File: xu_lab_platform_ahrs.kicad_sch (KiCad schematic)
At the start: 0 parts

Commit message: Add 9DoF IMU and magnetometer sensors to sheet
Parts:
- added U2: ICM-20948, Sensor_Motion:InvenSense_QFN-24_3x3mm_P0.4mm, symbol Sensor_Motion:ICM-20948
- added U3: MMC5603NJ, Package_BGA:WLP-4_0.82X0.82mm_MEM, symbol XuLab:MMC5603NJ
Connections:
- new net: U2.18 (GND), U2.20 (GND)
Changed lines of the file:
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@@
 		(company "CU Boulder Senior Design Team 29 - Xu Lab")
 	)
+	(symbol
+		(lib_id "Sensor_Motion:ICM-20948")
+		(at 107.95 93.98 0)
+		(unit 1)
+		(exclude_from_sim no)
+		(in_bom yes)
+		(on_board yes)
+		(dnp no)
+		(fields_autoplaced yes)
+		(property "Reference" "U2"
+			(at 110.0933 111.76 0)
+			(effects
+				(font
+					(size 1.27 1.27)
+				)
+				(justify left)
+			)
+		)
+		(property "Value" "ICM-20948"
+			(at 110.0933 114.3 0)
+			(effects
+				(font
+					(size 1.27 1.27)
+				)
+				(justify left)
+			)
+		)
+		(property "Footprint" "Sensor_Motion:InvenSense_QFN-24_3x3mm_P0.4mm"
+			(at 107.95 119.38 0)
+			(effects
+				(font
+					(size 1.27 1.27)
+				)
+				(hide yes)
+			)
+		)
+		(property "Datasheet" "http://www.invensense.com/wp-content/uploads/2016/06/DS-000189-ICM-20948-v1.3.pdf"
+			(at 107.95 97.79 0)
+			(effects
+				(font
+					(size 1.27 1.27)
+				)
+				(hide yes)
+			)
+		)
+		(property "Description" "InvenSense 9-Axis Motion Sensor, Accelerometer, Gyroscope, Compass, I2C/SPI, QFN-24"
+			(at 107.95 93.98 0)
+			(effects
+				(font
+					(size 1.27 1.27)
+				)
+				(hide yes)
+			)
+		)
+		(pin "24"
+		)
+		(pin "23"
+		)
+		(pin "22"
+		)
+		(pin "15"
+		)
+		(pin "11"
+		)
+		(pin "12"
+		)
+		(pin "1"
+		)
+		(pin "2"
+		)
+		(pin "3"
+		)
+		(pin "4"
+		)
+		(pin "5"
+		)
+		(pin "8"
+		)
+		(pin "18"
+		)
+		(pin "20"
+		)
+		(pin "13"
+		)
+		(pin "6"
+		)
+		(pin "14"
+		)
+		(pin "9"
+		)
+		(pin "16"
+		)
+		(pin "17"
+		)
+		(pin "19"
+		)
+		(pin "21"
+		)
+		(pin "7"
+		)
+		(pin "10"
+		)
+		(instances
+			(project ""
+				(path "/71bb14ae-b730-4d22-a41d-cf68989dae2d/a5713b00-422c-456a-9938-13721b057665"
+					(reference "U2")
+					(unit 1)
+				)
+			)
+		)
+	)
+	(symbol
+		(lib_id "XuLab:MMC5603NJ")
+		(at 170.18 95.25 0)
+		(unit 1)
+		(exclude_from_sim no)
+		(in_bom yes)
+		(on_board yes)
+		(dnp no)
+		(fields_autoplaced yes)
+		(property "Reference" "U3"
+			(at 170.18 83.82 0)
+			(effects
+				(font
+					(size 1.524 1.524)
+				)
+			)
+		)
+		(property "Value" "MMC5603NJ"
+			(at 170.18 86.36 0)
+			(effects
+				(font
+					(size 1.524 1.524)
+				)
+			)
+		)
+		(property "Footprint" "Package_BGA:WLP-4_0.82X0.82mm_MEM"
+			(at 170.434 104.902 0)
+			(effects
+				(font
+					(size 1.27 1.27)
+					(italic yes)
+				)
+				(hide yes)
+			)
+		)
+		(property "Datasheet" "https://mm.digikey.com/Volume0/opasdata/d220001/medias/docus/333/MMC5603NJ_RevB_7-12-18.pdf"
+			(at 170.18 102.87 0)
+			(effects
+				(font
+					(size 1.27 1.27)
+					(italic yes)
+				)
+				(hide yes)
+			)
+		)
+		(property "Description" "he MMC5603NJ is a monolithic complete 3-axis AMR magnetic sensor with on-chip signal processing and integrated digital bus"
+			(at 170.18 107.95 0)
+			(effects
+				(font
+					(size 1.27 1.27)
+				)
+				(hide yes)
+			)
+		)
+		(pin "A1"
+		)
+		(pin "B2"
+		)
+		(pin "A2"
+		)
+		(pin "B1"
+		)
+		(instances
+			(project ""
+				(path "/71bb14ae-b730-4d22-a41d-cf68989dae2d/a5713b00-422c-456a-9938-13721b057665"
+					(reference "U3")
+					(unit 1)
+				)
+			)
+		)
+	)
 )

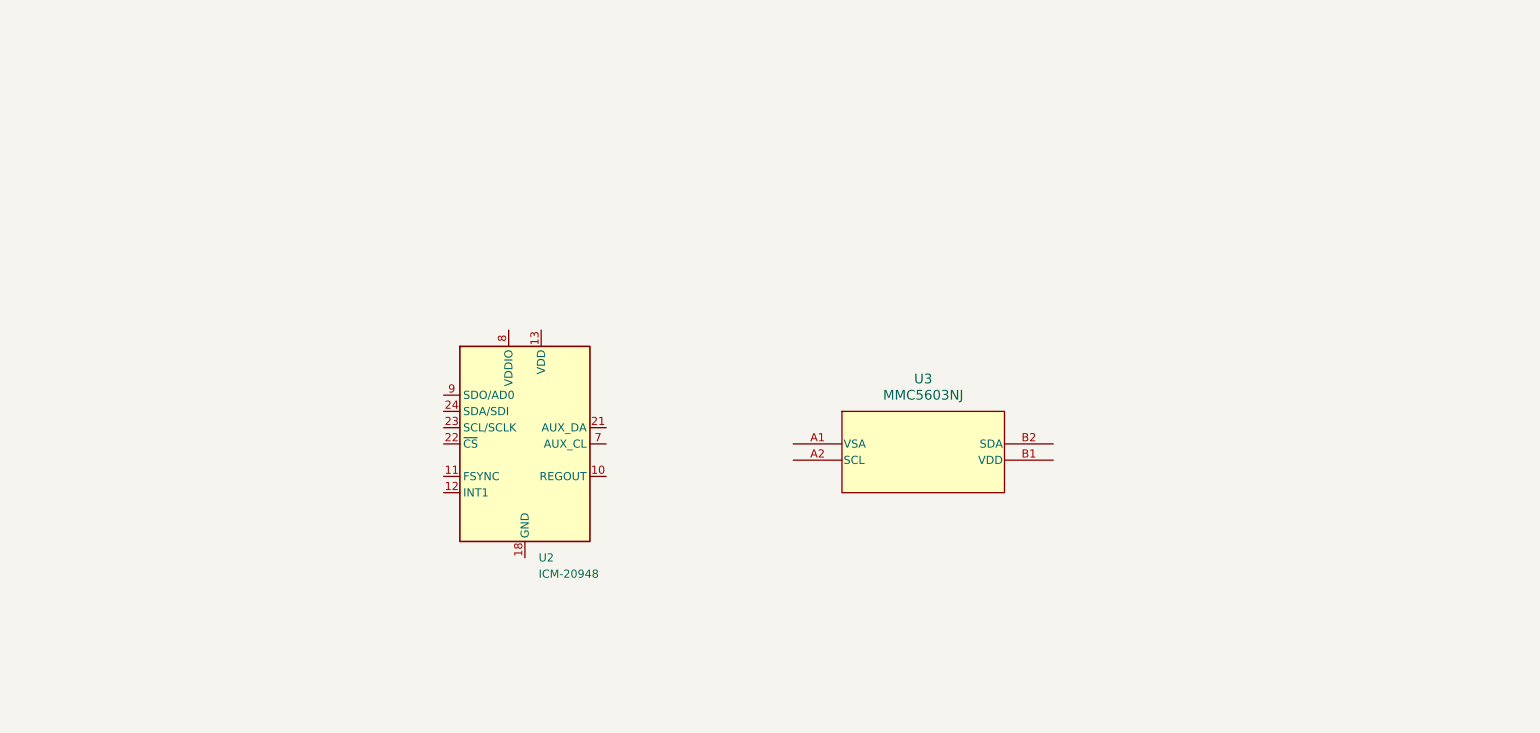
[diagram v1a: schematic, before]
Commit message: Add sensor connections
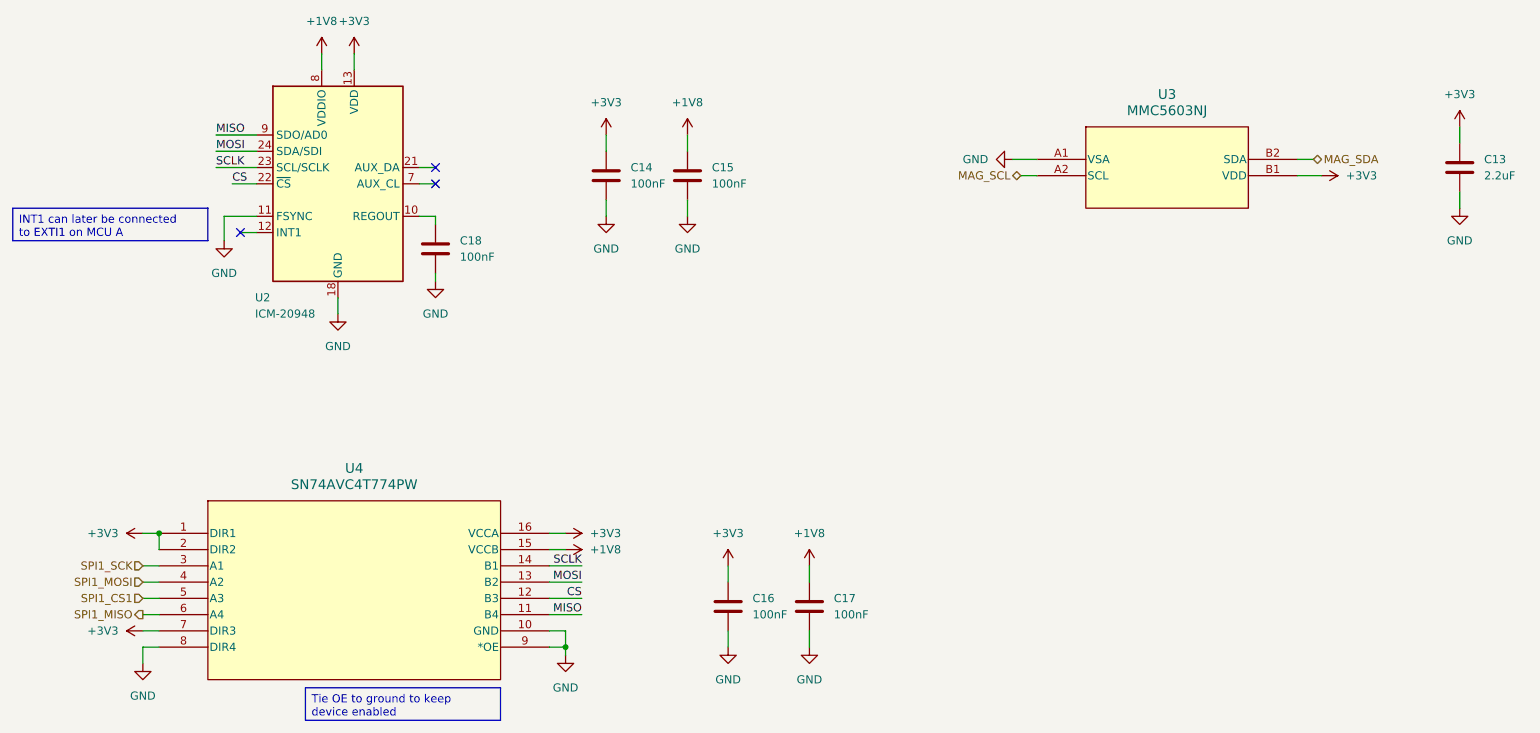
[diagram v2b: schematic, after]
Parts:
- added C13: 2.2uF, symbol Device:C
- added C14, C15, C16, C17, C18: 100nF, symbol Device:C
- added U4: SN74AVC4T774PW, PW16, symbol XuLab:SN74AVC4T774PW
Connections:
- net at U2.10 (REGOUT): now also C18.1
- net GND: now reaches U2.11 (FSYNC)
- net GND: now also U2.18 (GND), U2.20 (GND), U3.A1 (VSA), C13.2, C14.2, C15.2, C16.2, C17.2, C18.2, U4.10 (GND), U4.8 (DIR4), U4.9 (*OE)
- net +3V3: now reaches U2.13 (VDD)
- net +3V3: now also U3.B1 (VDD), C13.1, C14.1, C16.1, U4.1 (DIR1), U4.16 (VCCA), U4.2 (DIR2), U4.7 (DIR3)
- net CS: now reaches U2.22 (~{CS})
- net CS: now also U4.12 (B3)
- net SCLK: now reaches U2.23 (SCL/SCLK)
- net SCLK: now also U4.14 (B1)
- net MOSI: now reaches U2.24 (SDA/SDI)
- net MOSI: now also U4.13 (B2)
- net +1V8: now reaches U2.8 (VDDIO)
- net +1V8: now also C15.1, C17.1, U4.15 (VCCB)
- net MISO: now reaches U2.9 (SDO/AD0)
- net MISO: now also U4.11 (B4)
- net MAG_SCL: now reaches U3.A2 (SCL)
- net MAG_SDA: now reaches U3.B2 (SDA)
- new net SPI1_CS1: U4.5 (A3)
- new net SPI1_MISO: U4.6 (A4)
- new net SPI1_MOSI: U4.4 (A2)
- new net SPI1_SCK: U4.3 (A1)
- no-connect marks 0 -> 3
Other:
- moved on the sheet: U2, U3

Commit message: Add pressure sensor schematic
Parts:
- added C19: 100nF, symbol Device:C
- added J2: Conn_01x04, Connector_JST_GH:GH_B04B-GH-A_1x04_P1.25mm_Vertical, symbol Connector_Generic:Conn_01x04
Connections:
- net +3V3: now also C19.1
- net GND: now also C19.2, J2.4 (Pin_4)
- new net +3.3V: J2.1 (Pin_1)
- new net PS_SCL: J2.2 (Pin_2)
- new net PS_SDA: J2.3 (Pin_3)
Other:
- note added: "Bar30 Pressure Sensor Connector"
